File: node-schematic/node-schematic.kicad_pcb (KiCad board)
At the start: 2 copper layers, 23 parts, among them U1 NRF52840-QFAA-R7, X1 NX2016SA-32MHZ, X2 32.768kHz

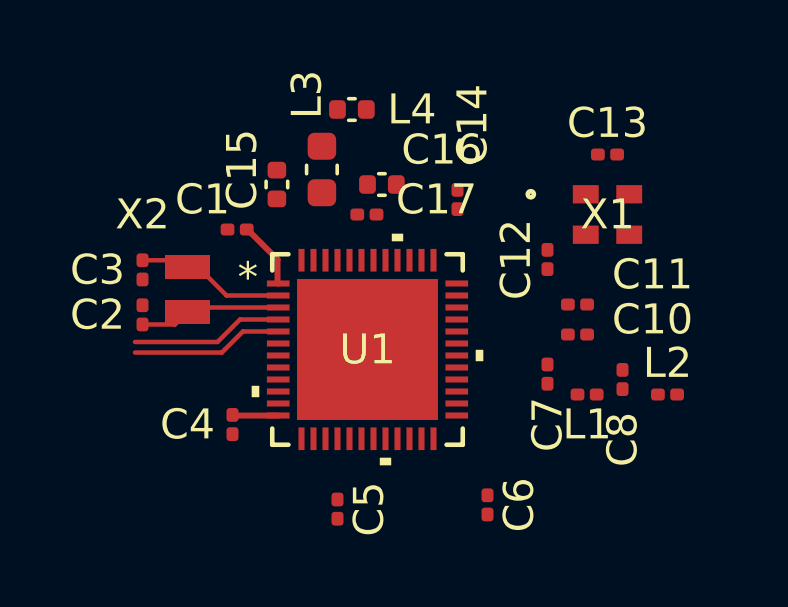
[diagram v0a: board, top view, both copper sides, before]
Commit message: added sx1262 sub page
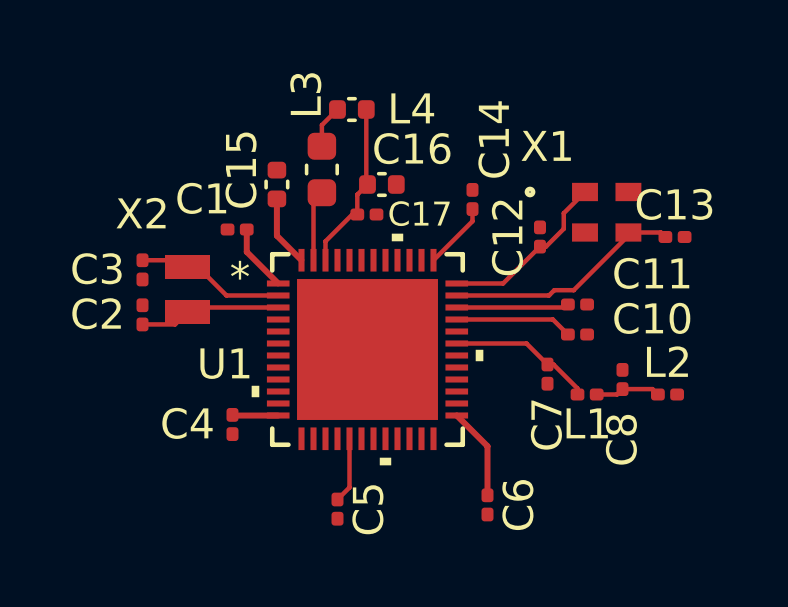
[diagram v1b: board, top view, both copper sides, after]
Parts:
- moved C13 3.55 mm to (161.8, 79.2)
- moved C12 0.79 mm to (157.2, 79.2)
- moved C14 0.50 mm to (155.0, 78.0)
- moved X1 0.08 mm to (159.5, 78.4)
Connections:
- C10 pad 1: GND -> /DEC4_6
- U1 pad 33: GND -> /DEC4_6
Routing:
- net VDD_nRF: track 1.53 -> 11.4 mm
- net Net-(U1-XC1): track 0.00 -> 7.97 mm
- net Net-(U1-XC2): track 0.00 -> 5.84 mm
- net Net-(U1-DEC4): track 0.00 -> 5.72 mm
- net unconnected-(U1-Pad4): track 5.09 -> 0.00 mm
- net unconnected-(U1-Pad5): track 5.06 -> 0.00 mm
- net Net-(U1-ANT): track 0.00 -> 4.85 mm
- net /DEC4_6: track 0.00 -> 3.91 mm
- net Net-(U1-DEC3): track 0.00 -> 3.75 mm
- net Net-(U1-DCC): track 0.00 -> 2.37 mm
- net Net-(C8-Pad1): track 0.00 -> 2.19 mm
- net Net-(L3-Pad2): track 0.00 -> 1.44 mm

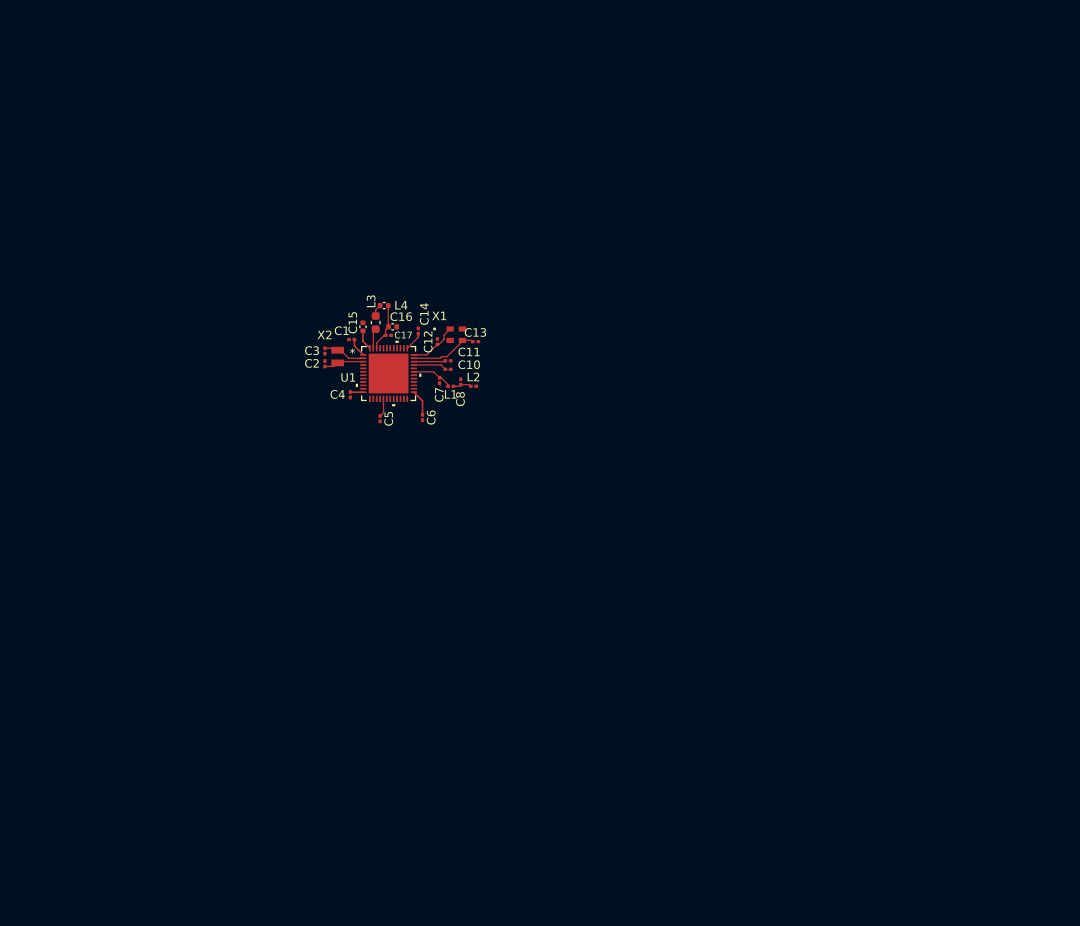
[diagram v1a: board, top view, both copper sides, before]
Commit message: fuel gauge implemented
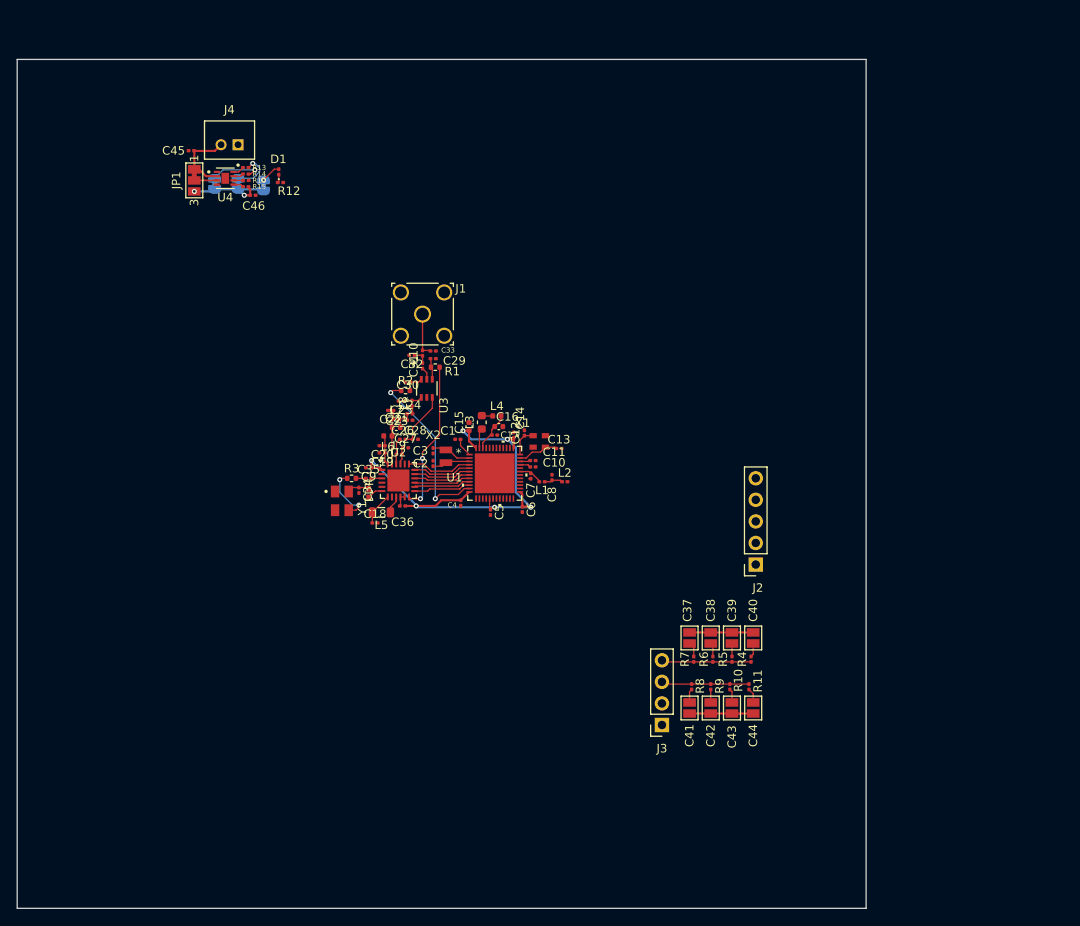
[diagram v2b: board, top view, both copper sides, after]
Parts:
- added C18: 470nF, Capacitor_SMD:C_0201_0603Metric, F.Cu at (149.9, 100.6)
- added C19: 100nF, Capacitor_SMD:C_0201_0603Metric, F.Cu at (150.8, 92.3)
- added C20: 47pF, Capacitor_SMD:C_0201_0603Metric, F.Cu at (150.8, 91.5)
- added C21: 3.0pF, Capacitor_SMD:C_0402_1005Metric, F.Cu at (152.4, 89.3)
- added C22: NC, Capacitor_SMD:C_0201_0603Metric, F.Cu at (151.8, 87.3)
- added C23: 5.6pF, Capacitor_SMD:C_0201_0603Metric, F.Cu at (154.0, 88.5)
- added C24: 39pF, Capacitor_SMD:C_0201_0603Metric, F.Cu at (154.0, 87.8)
- added C25: 3.3pF, Capacitor_SMD:C_0201_0603Metric, F.Cu at (153.0, 86.2)
- added C26: 2.4pF, Capacitor_SMD:C_0201_0603Metric, F.Cu at (153.2, 90.8)
- added C27: 1.8pF, Capacitor_SMD:C_0201_0603Metric, F.Cu at (153.5, 91.8)
- added C28: NC, Capacitor_SMD:C_0201_0603Metric, F.Cu at (154.7, 90.8)
- added C29: 1nF, Capacitor_SMD:C_0201_0603Metric, F.Cu at (156.8, 81.2)
- added C30: 1nF, Capacitor_SMD:C_0201_0603Metric, F.Cu at (153.8, 84.0)
- added C31: 39pF, Capacitor_SMD:C_0201_0603Metric, F.Cu at (155.5, 82.1)
- added C32: 3.9pF, Capacitor_SMD:C_0201_0603Metric, F.Cu at (154.2, 80.8)
- added C33: 3.9pF, Capacitor_SMD:C_0201_0603Metric, F.Cu at (156.8, 80.3)
- added C34: 100nF, Capacitor_SMD:C_0201_0603Metric, F.Cu at (148.0, 96.8)
- added C35: 10pF, Capacitor_SMD:C_0201_0603Metric, F.Cu at (149.1, 95.3)
- added C36: 100nF, Capacitor_SMD:C_0201_0603Metric, F.Cu at (153.2, 98.6)
- added C37: NC, Jumper:SolderJumper-2_P1.3mm_Open_Pad1.0x1.5mm, F.Cu at (186.9, 114.2)
- added C38: NC, Jumper:SolderJumper-2_P1.3mm_Open_Pad1.0x1.5mm, F.Cu at (189.4, 114.2)
- added C39: NC, Jumper:SolderJumper-2_P1.3mm_Open_Pad1.0x1.5mm, F.Cu at (191.9, 114.2)
- added C40: NC, Jumper:SolderJumper-2_P1.3mm_Open_Pad1.0x1.5mm, F.Cu at (194.4, 114.2)
- added C41: NC, Jumper:SolderJumper-2_P1.3mm_Open_Pad1.0x1.5mm, F.Cu at (186.9, 122.4)
- added C42: NC, Jumper:SolderJumper-2_P1.3mm_Open_Pad1.0x1.5mm, F.Cu at (189.4, 122.4)
- added C43: NC, Jumper:SolderJumper-2_P1.3mm_Open_Pad1.0x1.5mm, F.Cu at (191.9, 122.4)
- added C44: NC, Jumper:SolderJumper-2_P1.3mm_Open_Pad1.0x1.5mm, F.Cu at (194.4, 122.4)
- added C45: 1uF, Capacitor_SMD:C_0201_0603Metric, F.Cu at (128.3, 56.8)
- added C46: 1uF, Capacitor_SMD:C_0201_0603Metric, F.Cu at (135.5, 62.0)
- added C47: NC, Jumper:SolderJumper-2_P1.3mm_Bridged_RoundedPad1.0x1.5mm, B.Cu at (136.8, 60.9)
- added C48: NC, Jumper:SolderJumper-2_P1.3mm_Bridged_RoundedPad1.0x1.5mm, B.Cu at (133.8, 60.6)
- added C49: NC, Jumper:SolderJumper-2_P1.3mm_Bridged_RoundedPad1.0x1.5mm, B.Cu at (131.0, 60.6)
- added C9: 1uF, Capacitor_SMD:C_0201_0603Metric, F.Cu at (149.2, 94.1)
- added D1: GREEN, LED_SMD:LED_0201_0603Metric, F.Cu at (138.6, 59.2)
- added J1: SMA, RF2_04A_T_00_50_G:CONN_RF2-04A-T-00-50-G_ADM, F.Cu at (155.5, 76.0)
- added J2: SWD_DEBUG, Connector_PinSocket_2.54mm:PinSocket_1x05_P2.54mm_Vertical, F.Cu at (194.8, 105.5)
- added J3: I2C, Connector_PinSocket_2.54mm:PinSocket_1x04_P2.54mm_Vertical, F.Cu at (183.7, 124.4)
- added J4: B2B-PH-K-S, B2B_PH_K_S:JST_B2B-PH-K-S, F.Cu at (132.8, 55.5)
- added JP1: Power_select, Jumper:SolderJumper-3_P1.3mm_Bridged12_Pad1.0x1.5mm_NumberLabels, F.Cu at (128.6, 60.2)
- added L10: 9.1nH, Inductor_SMD:L_0201_0603Metric, F.Cu at (155.5, 80.6)
- added L11: 120@100MHz, BLM15AG121SN1D:IND_BLM15_0402_MUR, F.Cu at (149.2, 97.1)
- added L5: 15uH, Inductor_SMD:L_0805_2012Metric, F.Cu at (150.7, 99.3)
- added L6: 47nH, Inductor_SMD:L_0402_1005Metric, F.Cu at (151.4, 90.3)
- added L7: 2.5nH, Inductor_SMD:L_0201_0603Metric, F.Cu at (152.4, 88.3)
- added L8: 4.7nH, Inductor_SMD:L_0201_0603Metric, F.Cu at (154.2, 86.5)
- added L9: 15nH, Inductor_SMD:L_0201_0603Metric, F.Cu at (152.8, 92.5)
- added R1: 100R, Resistor_SMD:R_0402_1005Metric, F.Cu at (157.0, 82.2)
- added R10: 4.7k, Resistor_SMD:R_0201_0603Metric, F.Cu at (191.7, 119.9)
- added R11: 2.2k, Resistor_SMD:R_0201_0603Metric, F.Cu at (193.9, 119.9)
- added R12: 10K, Resistor_SMD:R_0201_0603Metric, F.Cu at (138.8, 60.5)
- added R13: 10K, Resistor_SMD:R_0201_0603Metric, F.Cu at (134.7, 58.8)
- added R14: 10K, Resistor_SMD:R_0201_0603Metric, F.Cu at (134.7, 59.5)
- added R15: 10k, Resistor_SMD:R_0201_0603Metric, F.Cu at (134.7, 61.0)
- added R16: 10k, Resistor_SMD:R_0201_0603Metric, F.Cu at (134.7, 60.2)
- added R2: 100R, Resistor_SMD:R_0402_1005Metric, F.Cu at (153.5, 85.0)
- added R3: 220, Resistor_SMD:R_0402_1005Metric, F.Cu at (147.1, 95.3)
- added R4: 2.2k, Resistor_SMD:R_0201_0603Metric, F.Cu at (194.2, 116.7)
- added R5: 4.7k, Resistor_SMD:R_0201_0603Metric, F.Cu at (191.9, 116.7)
- added R6: 6.8k, Resistor_SMD:R_0201_0603Metric, F.Cu at (189.7, 116.7)
- added R7: 10k, Resistor_SMD:R_0201_0603Metric, F.Cu at (187.4, 116.7)
- added R8: 10k, Resistor_SMD:R_0201_0603Metric, F.Cu at (187.2, 119.9)
- added R9: 6.8k, Resistor_SMD:R_0201_0603Metric, F.Cu at (189.4, 119.9)
- added U2: SX1262IMLTRT, Package_DFN_QFN:QFN-24-1EP_4x4mm_P0.5mm_EP2.6x2.6mm, F.Cu at (152.7, 95.6)
- added U3: 4259-63, 4259_63:SC-70-6_PSM, F.Cu at (156.0, 84.8)
- added U4: MAX17048G_T10, MAX17048G_T10:SON50P200X200X80-9N, F.Cu at (132.3, 60.0)
- added Y1: TX32-M010S-32.000-X-R, TX32_M010S_32_000_X_R:OSC_TX32-M010S-32.000-X-R, F.Cu at (146.0, 98.0)
- L3: footprint Capacitor_SMD:C_0603_1608Metric -> Inductor_SMD:L_0603_1608Metric
- L4: footprint Capacitor_SMD:C_0402_1005Metric -> Inductor_SMD:L_0402_1005Metric
- moved L4 18.6 mm to (164.2, 88.0)
- moved C4 18.2 mm to (160.0, 98.2)
- moved C2 17.3 mm to (156.8, 93.6)
- moved C3 17.3 mm to (156.8, 92.1)
- moved X2 17.3 mm to (158.2, 92.8)
- moved C1 17.2 mm to (159.7, 90.8)
- moved C15 17.2 mm to (161.0, 89.2)
- moved C16 17.2 mm to (164.5, 89.2)
- moved C17 17.2 mm to (164.0, 90.2)
- moved L3 17.2 mm to (162.5, 88.8)
- moved U1 17.2 mm to (164.0, 94.8)
- moved C5 17.0 mm to (163.5, 99.3)
- moved C14 16.6 mm to (166.2, 90.2)
- moved C6 16.0 mm to (167.2, 99.0)
- moved C13 16.0 mm to (171.6, 91.8)
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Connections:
- net VDD_nRF renamed VDD
- U1 pad 10: unconnected-(U1-Pad10) -> DIO1
- U1 pad 11: unconnected-(U1-Pad11) -> ANT_SW
- U1 pad 13: unconnected-(U1-P0.13-Pad13) -> I2C_SDA
- U1 pad 14: unconnected-(U1-P0.14-Pad14) -> I2C_SCL
- U1 pad 16: unconnected-(U1-Pad16) -> RESET
- U1 pad 24: unconnected-(U1-Pad24) -> SWO
- U1 pad 4: unconnected-(U1-Pad4) -> SPI_NSS
- U1 pad 5: unconnected-(U1-Pad5) -> SPI_CLK
- U1 pad 6: unconnected-(U1-Pad6) -> SPI_MOSI
- U1 pad 7: unconnected-(U1-P0.08-Pad7) -> SPI_MISO
- U1 pad 8: unconnected-(U1-P1.08-Pad8) -> NRESET
- U1 pad 9: unconnected-(U1-Pad9) -> BUSY
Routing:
- net VDD: track 11.4 -> 82.1 mm, vias 0 -> 8
- net ANT_SW: track 0.00 -> 20.5 mm, vias 0 -> 2
- net DIO2: track 0.00 -> 17.9 mm, vias 0 -> 2
- net I2C_SCL: track 0.00 -> 10.6 mm
- net I2C_SDA: track 0.00 -> 10.4 mm
- net VBUS: track 0.00 -> 8.66 mm
- net SPI_NSS: track 0.00 -> 7.78 mm
- net SPI_CLK: track 0.00 -> 6.93 mm
- net Net-(Y1-OUTPUT): track 0.00 -> 6.91 mm, vias 0 -> 2
- net SPI_MOSI: track 0.00 -> 6.85 mm
- net SPI_MISO: track 0.00 -> 6.77 mm
- net Net-(U3-RF2): track 0.00 -> 6.75 mm
- net DIO1: track 0.00 -> 6.73 mm
- net NRESET: track 0.00 -> 6.69 mm
- net BUSY: track 0.00 -> 6.69 mm
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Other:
- board outline added: 100 x 100 mm

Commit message: completed pcb and box
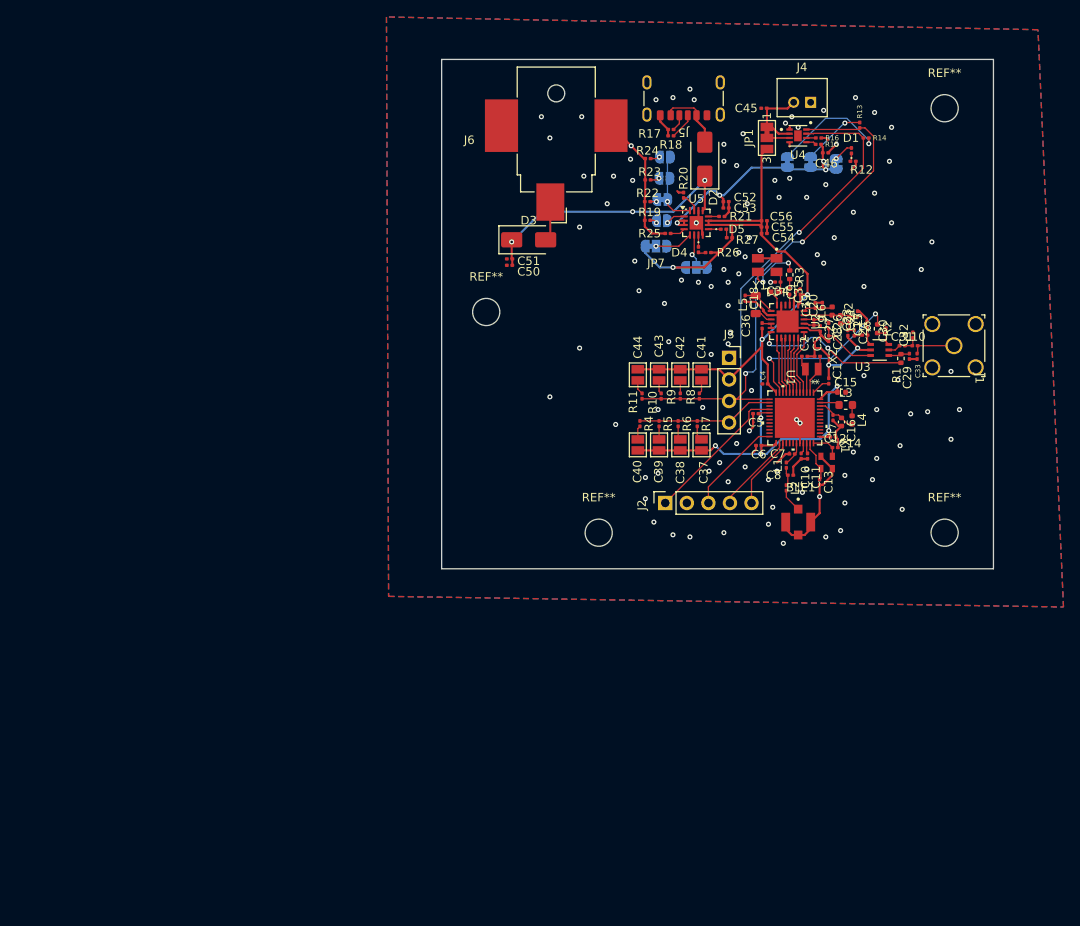
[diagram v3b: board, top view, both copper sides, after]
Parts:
- added 0.5A1: 0.5A, Jumper:SolderJumper-2_P1.3mm_Bridged_RoundedPad1.0x1.5mm, B.Cu at (183.8, 62.5)
- added 1.5A1: 1.5A, Jumper:SolderJumper-2_P1.3mm_Open_RoundedPad1.0x1.5mm, B.Cu at (184.1, 57.5)
- added 1A1: 1A, Jumper:SolderJumper-2_P1.3mm_Open_RoundedPad1.0x1.5mm, B.Cu at (184.0, 60.0)
- added BLE1: CONMHF1-SMD-G-T, CONMHF1_SMD_G_T:LINX_CONMHF1-SMD-G-T, F.Cu at (199.8, 100.5)
- added C50: 10uF, Capacitor_SMD:C_0201_0603Metric, F.Cu at (165.8, 70.2)
- added C51: 10uF, Capacitor_SMD:C_0201_0603Metric, F.Cu at (165.8, 69.5)
- added C52: 10uF, Capacitor_SMD:C_0201_0603Metric, F.Cu at (191.2, 62.8)
- added C53: 10uF, Capacitor_SMD:C_0201_0603Metric, F.Cu at (191.2, 63.5)
- added C54: 10uF, Capacitor_SMD:C_0201_0603Metric, F.Cu at (195.8, 66.5)
- added C55: 10uF, Capacitor_SMD:C_0201_0603Metric, F.Cu at (195.8, 65.8)
- added C56: 10uF, Capacitor_SMD:C_0201_0603Metric, F.Cu at (195.8, 65.0)
- added D2: MBRA340, Diode_SMD:D_SMA, F.Cu at (188.8, 57.8)
- added D3: MBRA340, Diode_SMD:D_SMA, F.Cu at (168.0, 67.2)
- added D4: PGOOD (GREEN), LED_SMD:LED_0201_0603Metric, F.Cu at (188.0, 68.4)
- added D5: CHG (RED), LED_SMD:LED_0201_0603Metric, F.Cu at (191.0, 66.0)
- added J5: USB_C_Receptacle_PowerOnly_6P, Connector_USB:USB_C_Receptacle_GCT_USB4125-xx-x_6P_TopMnt_Horizontal, F.Cu at (186.2, 49.5)
- added J6: Barrel_Jack, Connector_BarrelJack:BarrelJack_CUI_PJ-036AH-SMT_Horizontal, F.Cu at (171.2, 57.0)
- added JP2: THERM, Jumper:SolderJumper-2_P1.3mm_Open_RoundedPad1.0x1.5mm, B.Cu at (183.7, 65.0)
- added JP6: EN1, Jumper:SolderJumper-3_P1.3mm_Bridged12_RoundedPad1.0x1.5mm_NumberLabels, B.Cu at (187.8, 70.5)
- added JP7: EN2, Jumper:SolderJumper-3_P1.3mm_Bridged12_RoundedPad1.0x1.5mm_NumberLabels, B.Cu at (183.0, 68.0)
- added R17: 5.1K, Resistor_SMD:R_0201_0603Metric, F.Cu at (184.8, 54.2)
- added R18: 5.1K, Resistor_SMD:R_0201_0603Metric, F.Cu at (184.8, 55.0)
- added R19: 10K, Resistor_SMD:R_0201_0603Metric, F.Cu at (182.0, 65.0)
- added R20: 10K, Resistor_SMD:R_0201_0603Metric, F.Cu at (186.2, 62.0)
- added R21: 1K, Resistor_SMD:R_0201_0603Metric, F.Cu at (190.8, 64.5)
- added R22: 2K, Resistor_SMD:R_0201_0603Metric, F.Cu at (182.0, 62.8)
- added R23: 1K, Resistor_SMD:R_0201_0603Metric, F.Cu at (182.1, 60.2)
- added R24: 590, Resistor_SMD:R_0201_0603Metric, F.Cu at (182.1, 57.7)
- added R25: 10K, Resistor_SMD:R_0201_0603Metric, F.Cu at (184.4, 66.5)
- added R26: 10K, Resistor_SMD:R_0201_0603Metric, F.Cu at (189.2, 68.8)
- added R27: 10K, Resistor_SMD:R_0201_0603Metric, F.Cu at (191.7, 67.0)
- added REF**: MountingHole_3.2mm_M3, MountingHole:MountingHole_3.2mm_M3, F.Cu at (176.2, 101.8)
- added REF**: MountingHole_3.2mm_M3, MountingHole:MountingHole_3.2mm_M3, F.Cu at (217.0, 101.8)
- added REF**: MountingHole_3.2mm_M3, MountingHole:MountingHole_3.2mm_M3, F.Cu at (217.0, 51.8)
- added REF**: MountingHole_3.2mm_M3, MountingHole:MountingHole_3.2mm_M3, F.Cu at (163.0, 75.8)
- added U5: BQ24074RGT, Package_DFN_QFN:VQFN-16-1EP_3x3mm_P0.5mm_EP1.6x1.6mm, F.Cu at (187.8, 65.2)
- moved R14 73.2 mm to (207.8, 55.2)
- moved R13 72.5 mm to (207.0, 53.8), turned to -90 degrees
- moved C45 67.6 mm to (195.7, 51.8)
- moved C46 67.6 mm to (203.0, 57.0)
- moved J4 67.6 mm to (200.2, 50.5)
- moved R15 67.6 mm to (202.1, 56.0)
- moved R16 67.6 mm to (202.2, 55.2)
- moved U4 67.6 mm to (199.7, 55.0)
- moved JP1 67.6 mm to (196.1, 55.2)
- moved C47 67.5 mm to (204.2, 58.3)
- moved C48 67.5 mm to (201.2, 58.1)
- moved C49 67.5 mm to (198.5, 58.1)
- moved D1 67.5 mm to (206.0, 56.8)
- moved R12 67.5 mm to (206.2, 58.0)
- moved J1 62.7 mm to (218.1, 79.7), turned to -90 degrees
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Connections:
- net VBUS renamed VBAT
- C46 pad 1: VDD -> VFUEL
- C47 pad 1: VDD -> VFUEL
- C48 pad 1: VDD -> VFUEL
- C49 pad 1: VDD -> VFUEL
- J2 pad 4: SWDCLK -> SWDIO
- J2 pad 5: SWDIO -> SWDCLK
- L2 pad 2: RF -> Net-(BLE1-Pad1)
- R13 pad 2: MAX_SDA -> I2C_SDA
- R14 pad 2: MAX_SCL -> I2C_SCL
- R15 pad 2: VDD -> VFUEL
- U4 pad 7: MAX_SCL -> I2C_SCL
- U4 pad 8: MAX_SDA -> I2C_SDA
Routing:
- net GND: track 0.20 -> 102.1 mm, vias 0 -> 110
- net VDD: track 82.1 -> 139.4 mm
- net I2C_SCL: track 10.6 -> 63.7 mm, vias 0 -> 1
- net I2C_SDA: track 10.4 -> 62.2 mm, vias 0 -> 2
- net VBUS: track 0.00 -> 32.9 mm, vias 0 -> 3
- net VFUEL: track 0.00 -> 30.1 mm, vias 0 -> 4
- net RESET: track 0.00 -> 17.4 mm
- net SWO: track 0.00 -> 11.6 mm
- net SWDIO: track 0.00 -> 9.47 mm
- net SWDCLK: track 0.00 -> 8.58 mm
- net Net-(0.5A1-B): track 0.00 -> 8.37 mm, vias 0 -> 1
- net Net-(D2-A): track 0.00 -> 8.00 mm
- net Net-(C49-Pad2): track 6.12 -> 13.6 mm
- net Net-(D3-A): track 0.00 -> 4.68 mm
- net Net-(JP7-C): track 0.00 -> 4.54 mm, vias 0 -> 1
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- added copper zone on B.Cu, net GND
- added copper zone on F.Cu, net GND
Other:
- board size 100 x 100 mm -> 65 x 60 mm
